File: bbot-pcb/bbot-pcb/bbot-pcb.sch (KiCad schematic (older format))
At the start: 11 parts, among them U1 HA-552-4P, U2 ADXL335, U3 HA-552-4P, U4 OPENLOG

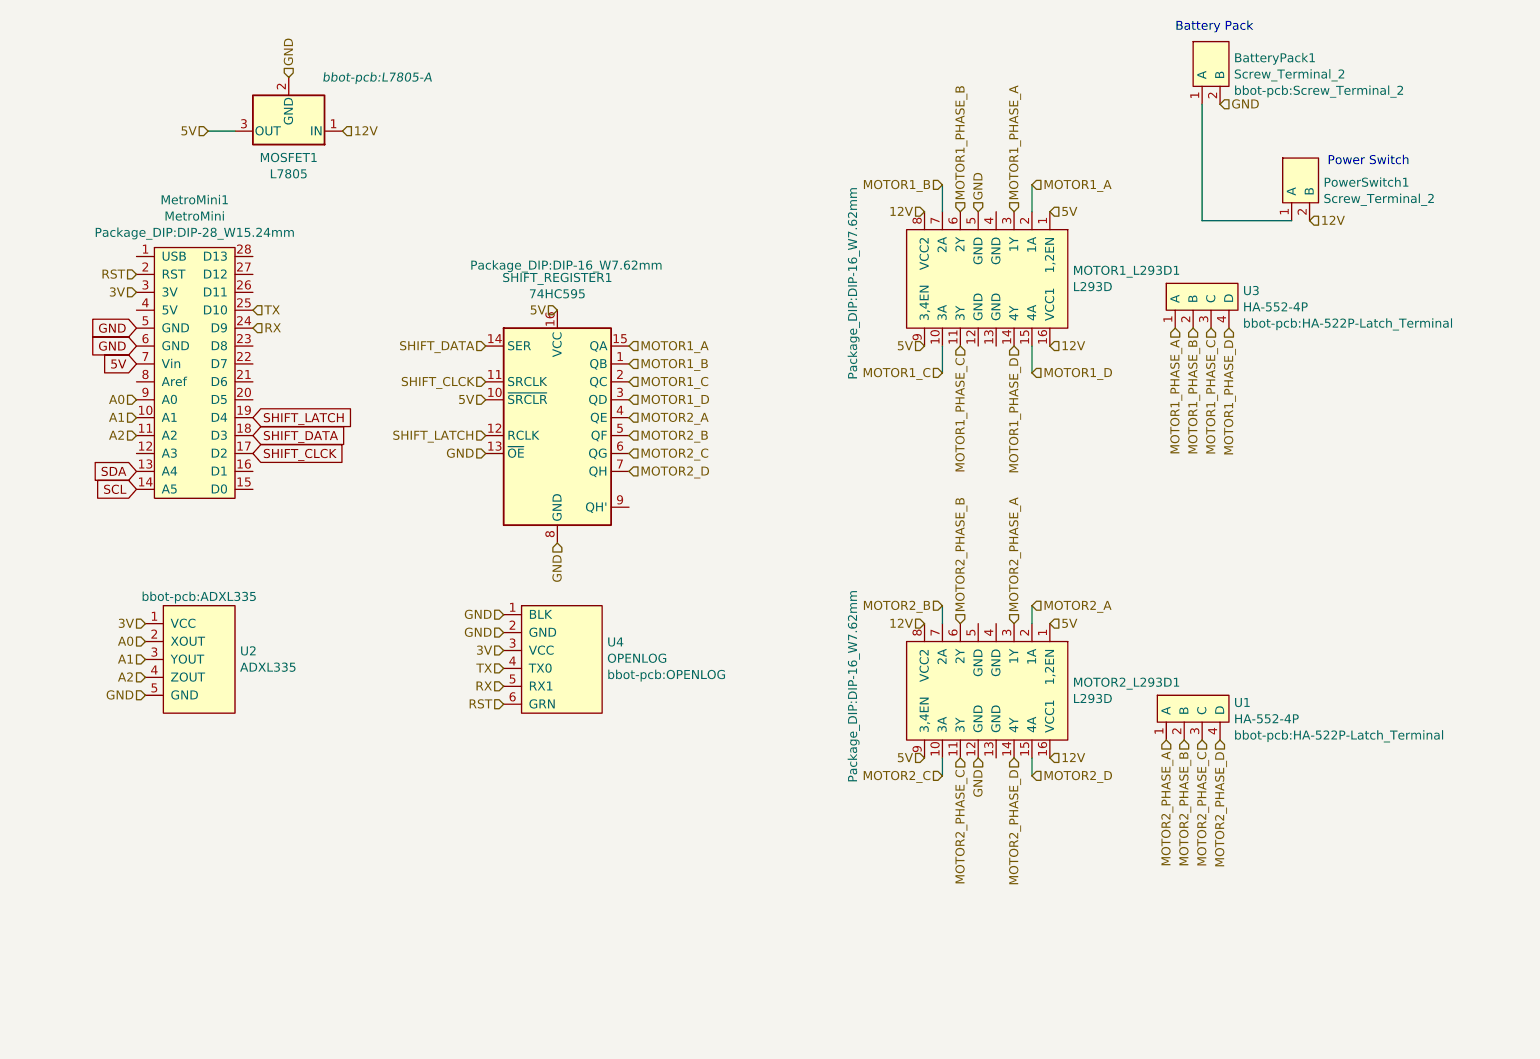
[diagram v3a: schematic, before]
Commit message: Update PCB to v3
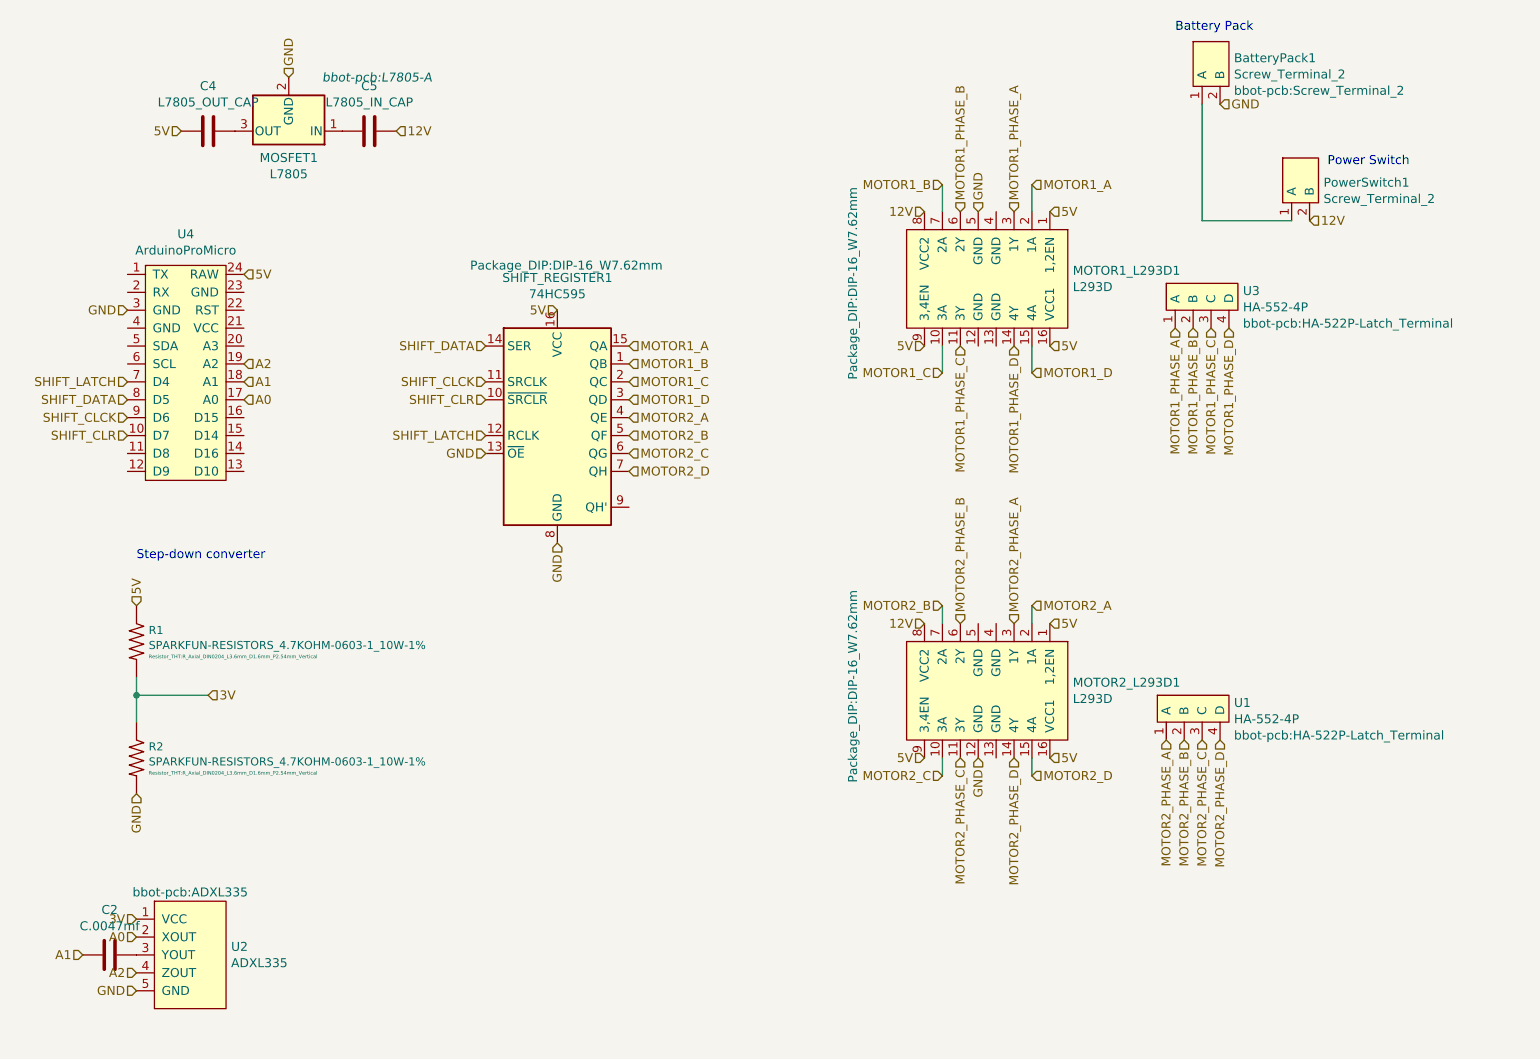
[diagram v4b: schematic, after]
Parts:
- removed MetroMini1: MetroMini, Package_DIP:DIP-28_W15.24mm, symbol bbot-component-library:MetroMini
- removed U4: OPENLOG, bbot-pcb:OPENLOG, symbol bbot-component-library:OPENLOG
- added C2: C.0047mf, Capacitor_THT:C_Disc_D3.4mm_W2.1mm_P2.50mm, symbol Device:C
- added C4: L7805_OUT_CAP, Capacitor_THT:CP_Radial_D5.0mm_P2.50mm, symbol Device:C
- added C5: L7805_IN_CAP, Capacitor_THT:CP_Radial_D5.0mm_P2.50mm, symbol Device:C
- added R1, R2: SPARKFUN-RESISTORS_4.7KOHM-0603-1_10W-1%, Resistor_THT:R_Axial_DIN0204_L3.6mm_D1.6mm_P2.54mm_Vertical, symbol Sparkfun:SPARKFUN-RESISTORS_4.7KOHM-0603-1_10W-1%
- added U4: ArduinoProMicro, promicro:ProMicro, symbol bbot-component-library:ArduinoProMicro
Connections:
- net 12V: now also C5.1; no longer MOSFET1.1 (IN), MOTOR1_L293D1.16 (VCC1), MOTOR2_L293D1.16 (VCC1)
- net 3V: now also R1.2, R2.1
- net 5V: now also MOTOR1_L293D1.16 (VCC1), MOTOR2_L293D1.16 (VCC1), C4.2, R1.1, U4.24 (RAW); no longer MOSFET1.3 (OUT), SHIFT_REGISTER1.10 (~SRCLR)
- net A0: now also U4.17 (A0)
- net A1: now also C2.2, U4.18 (A1); no longer U2.3 (YOUT)
- net A2: now also U4.19 (A2)
- net GND: now also R2.2, U4.3 (GND)
- net SHIFT_CLCK: now also U4.9 (D6)
- net SHIFT_DATA: now also U4.8 (D5)
- net SHIFT_LATCH: now also U4.7 (D4)
- new net: C5.2, MOSFET1.1 (IN)
- new net: C4.1, MOSFET1.3 (OUT)
- new net: C2.1, U2.3 (YOUT)
- new net SHIFT_CLR: SHIFT_REGISTER1.10 (~SRCLR), U4.10 (D7)
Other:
- note added: "Step-down converter"
- moved on the sheet: U2
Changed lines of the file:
@@
 Text HLabel 5900 1600 1    50   Input ~ 0
 GND
-Text HLabel 3550 3450 3    50   Input ~ 0
-GND
 Text HLabel 2050 850  1    50   Input ~ 0
 GND
-Text HLabel 2350 1150 2    50   Input ~ 0
+Text HLabel 2650 1150 2    50   Input ~ 0
 12V
 Text HLabel 6300 2350 2    50   Input ~ 0
-12V
+5V
 Text HLabel 5600 1600 0    50   Input ~ 0
 12V
 Text HLabel 6300 4650 2    50   Input ~ 0
-12V
+5V
 Text HLabel 5600 3900 0    50   Input ~ 0
 12V
-Wire Wire Line
-	1750 1150 1600 1150
-Text HLabel 1600 1150 0    50   Input ~ 0
+Text HLabel 1450 1150 0    50   Input ~ 0
 5V
 Text HLabel 3550 2150 0    50   Input ~ 0
@@
 SHIFT_CLCK
 Text HLabel 3150 2650 0    50   Input ~ 0
-5V
+SHIFT_CLR
 Text HLabel 3150 2950 0    50   Input ~ 0
 GND
@@
 Wire Wire Line
 	7150 1650 7650 1650
-$Comp
-L bbot-component-library:MetroMini MetroMini1
-U 1 1 6072CA85
-P 1550 2500
-F 0 "MetroMini1" H 1525 3465 50  0000 C CNN
-F 1 "MetroMini" H 1525 3374 50  0000 C CNN
-F 2 "Package_DIP:DIP-28_W15.24mm" H 1525 3283 50  0000 C CNN
-F 3 "" H 1300 2850 50  0001 C CNN
-	1    1550 2500
-	1    0    0    -1
-$EndComp
-Text GLabel 1200 2450 0    50   Input ~ 0
-5V
-Text GLabel 1850 2950 2    50   Input ~ 0
-SHIFT_CLCK
-Text GLabel 1850 2850 2    50   Input ~ 0
-SHIFT_DATA
-Text GLabel 1850 2750 2    50   Input ~ 0
-SHIFT_LATCH
-Text GLabel 1200 2250 0    50   Input ~ 0
-GND
-Text GLabel 1200 2350 0    50   Input ~ 0
-GND
-Text GLabel 1200 3050 0    50   Input ~ 0
-SDA
-Text GLabel 1200 3150 0    50   Input ~ 0
-SCL
 Wire Wire Line
 	5700 2350 5700 2500
@@
 L bbot-component-library:ADXL335 U2
 U 1 1 607BD863
-P 1500 3950
-F 0 "U2" H 1778 3846 50  0000 L CNN
-F 1 "ADXL335" H 1778 3755 50  0000 L CNN
-F 2 "bbot-pcb:ADXL335" H 1550 4150 50  0000 C CNN
-F 3 "" H 1250 4000 50  0001 C CNN
-	1    1500 3950
-	1    0    0    -1
-$EndComp
-Text HLabel 1250 3900 0    50   Input ~ 0
+P 1450 5600
+F 0 "U2" H 1728 5496 50  0000 L CNN
+F 1 "ADXL335" H 1728 5405 50  0000 L CNN
+F 2 "bbot-pcb:ADXL335" H 1500 5800 50  0000 C CNN
+F 3 "" H 1200 5650 50  0001 C CNN
+	1    1450 5600
+	1    0    0    -1
+$EndComp
+Text HLabel 1200 5550 0    50   Input ~ 0
 3V
-Text HLabel 1250 4000 0    50   Input ~ 0
+Text HLabel 1200 5650 0    50   Input ~ 0
 A0
-Text HLabel 1250 4100 0    50   Input ~ 0
+Text HLabel 900  5750 0    50   Input ~ 0
 A1
-Text HLabel 1250 4200 0    50   Input ~ 0
+Text HLabel 1200 5850 0    50   Input ~ 0
 A2
-Text HLabel 1250 4300 0    50   Input ~ 0
-GND
-Text HLabel 1200 2650 0    50   Input ~ 0
+Text HLabel 1200 5950 0    50   Input ~ 0
+GND
+Text HLabel 3550 3450 3    50   Input ~ 0
+GND
+$Comp
+L bbot-component-library:ArduinoProMicro U4
+U 1 1 608BA4F8
+P 1550 2450
+F 0 "U4" H 1475 3175 50  0000 C CNN
+F 1 "ArduinoProMicro" H 1475 3084 50  0000 C CNN
+F 2 "promicro:ProMicro" H 1250 3250 50  0001 C CNN
+F 3 "" H 1250 3250 50  0001 C CNN
+	1    1550 2450
+	1    0    0    -1
+$EndComp
+$Comp
+L Sparkfun:SPARKFUN-RESISTORS_4.7KOHM-0603-1_10W-1% R1
+U 1 1 608BCB4A
+P 1200 4000
+F 0 "R1" V 1137 4068 45  0000 L CNN
+F 1 "SPARKFUN-RESISTORS_4.7KOHM-0603-1_10W-1%" V 1221 4068 45  0000 L CNN
+F 2 "Resistor_THT:R_Axial_DIN0204_L3.6mm_D1.6mm_P2.54mm_Vertical" V 1284 4068 20  0000 L CNN
+F 3 "" H 1200 4000 60  0001 C CNN
+	1    1200 4000
+	0    1    1    0
+$EndComp
+$Comp
+L Sparkfun:SPARKFUN-RESISTORS_4.7KOHM-0603-1_10W-1% R2
+U 1 1 608BDF88
+P 1200 4650
+F 0 "R2" V 1137 4718 45  0000 L CNN
+F 1 "SPARKFUN-RESISTORS_4.7KOHM-0603-1_10W-1%" V 1221 4718 45  0000 L CNN
+F 2 "Resistor_THT:R_Axial_DIN0204_L3.6mm_D1.6mm_P2.54mm_Vertical" V 1284 4718 20  0000 L CNN
+F 3 "" H 1200 4650 60  0001 C CNN
+	1    1200 4650
+	0    1    1    0
+$EndComp
+Text HLabel 1200 4850 3    50   Input ~ 0
+GND
+Text HLabel 1200 3800 1    50   Input ~ 0
+5V
+Wire Wire Line
+	1200 4200 1200 4300
+Wire Wire Line
+	1200 4300 1600 4300
+Connection ~ 1200 4300
+Wire Wire Line
+	1200 4300 1200 4450
+Text HLabel 1600 4300 2    50   Input ~ 0
+3V
+Text HLabel 1800 1950 2    50   Input ~ 0
+5V
+Text HLabel 1150 2150 0    50   Input ~ 0
+GND
+Text HLabel 1800 2650 2    50   Input ~ 0
 A0
-Text HLabel 1200 2750 0    50   Input ~ 0
+Text HLabel 1800 2550 2    50   Input ~ 0
 A1
-Text HLabel 1200 2850 0    50   Input ~ 0
+Text HLabel 1800 2450 2    50   Input ~ 0
 A2
-Text HLabel 1200 2050 0    50   Input ~ 0
-3V
-$Comp
-L bbot-component-library:OPENLOG U4
-U 1 1 607C091B
-P 3550 4050
-F 0 "U4" H 3828 4096 50  0000 L CNN
-F 1 "OPENLOG" H 3828 4005 50  0000 L CNN
-F 2 "bbot-pcb:OPENLOG" H 3828 3914 50  0000 L CNN
-F 3 "" H 3250 4250 50  0001 C CNN
-	1    3550 4050
-	1    0    0    -1
-$EndComp
-Text HLabel 3250 4050 0    50   Input ~ 0
-3V
-Text HLabel 3250 3950 0    50   Input ~ 0
-GND
-Text HLabel 3250 3850 0    50   Input ~ 0
-GND
-Text HLabel 3250 4150 0    50   Input ~ 0
-TX
-Text HLabel 3250 4250 0    50   Input ~ 0
-RX
-Text HLabel 1850 2150 2    50   Input ~ 0
-TX
-Text HLabel 1850 2250 2    50   Input ~ 0
-RX
-Text HLabel 3250 4350 0    50   Input ~ 0
-RST
-Text HLabel 1200 1950 0    50   Input ~ 0
-RST
+Text Notes 1200 3550 0    50   ~ 0
+Step-down converter
+Text HLabel 1150 2550 0    50   Input ~ 0
+SHIFT_LATCH
+Text HLabel 1150 2650 0    50   Input ~ 0
+SHIFT_DATA
+Text HLabel 1150 2750 0    50   Input ~ 0
+SHIFT_CLCK
+Text HLabel 1150 2850 0    50   Input ~ 0
+SHIFT_CLR
+$Comp
+L Device:C C2
+U 1 1 608C7BCB
+P 1050 5750
+F 0 "C2" V 798 5750 50  0000 C CNN
+F 1 "C.0047mf" V 889 5750 50  0000 C CNN
+F 2 "Capacitor_THT:C_Disc_D3.4mm_W2.1mm_P2.50mm" H 1088 5600 50  0001 C CNN
+F 3 "~" H 1050 5750 50  0001 C CNN
+	1    1050 5750
+	0    1    1    0
+$EndComp
+$Comp
+L Device:C C4
+U 1 1 608C879A
+P 1600 1150
+F 0 "C4" V 1348 1150 50  0000 C CNN
+F 1 "L7805_OUT_CAP" V 1439 1150 50  0000 C CNN
+F 2 "Capacitor_THT:CP_Radial_D5.0mm_P2.50mm" H 1638 1000 50  0001 C CNN
+F 3 "~" H 1600 1150 50  0001 C CNN
+	1    1600 1150
+	0    1    1    0
+$EndComp
+$Comp
+L Device:C C5
+U 1 1 608C9E4F
+P 2500 1150
+F 0 "C5" V 2248 1150 50  0000 C CNN
+F 1 "L7805_IN_CAP" V 2339 1150 50  0000 C CNN
+F 2 "Capacitor_THT:CP_Radial_D5.0mm_P2.50mm" H 2538 1000 50  0001 C CNN
+F 3 "~" H 2500 1150 50  0001 C CNN
+	1    2500 1150
+	0    1    1    0
+$EndComp
 $EndSCHEMATC

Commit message: RElease-candidate of models and pcb
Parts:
- C4, C5: footprint Capacitor_THT:CP_Radial_D5.0mm_P2.50mm -> Capacitor_THT:C_Disc_D4.3mm_W1.9mm_P5.00mm
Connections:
- net 12V: now also MOSFET1.1 (IN)
- net 5V: now also C4.1, MOSFET1.3 (OUT); no longer C4.2
- net A1: now also C2.1, U2.3 (YOUT); no longer C2.2
- net GND: now also C2.2, C4.2, C5.2
- net SHIFT_CLCK: now also U4.8 (D5); no longer U4.9 (D6)
- net SHIFT_CLR: now also U4.7 (D4); no longer U4.10 (D7)
- net SHIFT_DATA: now also U4.10 (D7); no longer U4.8 (D5)
- net SHIFT_LATCH: now also U4.9 (D6); no longer U4.7 (D4)
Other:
- moved on the sheet: C2, C4, C5
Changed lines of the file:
@@
 Text HLabel 5600 3900 0    50   Input ~ 0
 12V
-Text HLabel 1450 1150 0    50   Input ~ 0
+Text HLabel 1550 1150 0    50   Input ~ 0
 5V
 Text HLabel 3550 2150 0    50   Input ~ 0
@@
 Text HLabel 1200 5650 0    50   Input ~ 0
 A0
-Text HLabel 900  5750 0    50   Input ~ 0
+Text HLabel 700  5700 0    50   Input ~ 0
 A1
 Text HLabel 1200 5850 0    50   Input ~ 0
@@
 Text Notes 1200 3550 0    50   ~ 0
 Step-down converter
+Text HLabel 1150 2750 0    50   Input ~ 0
+SHIFT_LATCH
+Text HLabel 1150 2850 0    50   Input ~ 0
+SHIFT_DATA
+Text HLabel 1150 2650 0    50   Input ~ 0
+SHIFT_CLCK
 Text HLabel 1150 2550 0    50   Input ~ 0
-SHIFT_LATCH
-Text HLabel 1150 2650 0    50   Input ~ 0
-SHIFT_DATA
-Text HLabel 1150 2750 0    50   Input ~ 0
-SHIFT_CLCK
-Text HLabel 1150 2850 0    50   Input ~ 0
 SHIFT_CLR
 $Comp
 L Device:C C2
 U 1 1 608C7BCB
-P 1050 5750
-F 0 "C2" V 798 5750 50  0000 C CNN
-F 1 "C.0047mf" V 889 5750 50  0000 C CNN
-F 2 "Capacitor_THT:C_Disc_D3.4mm_W2.1mm_P2.50mm" H 1088 5600 50  0001 C CNN
-F 3 "~" H 1050 5750 50  0001 C CNN
-	1    1050 5750
-	0    1    1    0
+P 900 5850
+F 0 "C2" V 648 5850 50  0000 C CNN
+F 1 "C.0047mf" V 739 5850 50  0000 C CNN
+F 2 "Capacitor_THT:C_Disc_D3.4mm_W2.1mm_P2.50mm" H 938 5700 50  0001 C CNN
+F 3 "~" H 900 5850 50  0001 C CNN
+	1    900  5850
+	1    0    0    -1
 $EndComp
 $Comp
 L Device:C C4
 U 1 1 608C879A
-P 1600 1150
-F 0 "C4" V 1348 1150 50  0000 C CNN
-F 1 "L7805_OUT_CAP" V 1439 1150 50  0000 C CNN
-F 2 "Capacitor_THT:CP_Radial_D5.0mm_P2.50mm" H 1638 1000 50  0001 C CNN
-F 3 "~" H 1600 1150 50  0001 C CNN
-	1    1600 1150
-	0    1    1    0
+P 1600 1300
+F 0 "C4" V 1348 1300 50  0000 C CNN
+F 1 "L7805_OUT_CAP" V 1250 1300 50  0000 C CNN
+F 2 "Capacitor_THT:C_Disc_D4.3mm_W1.9mm_P5.00mm" H 1638 1150 50  0001 C CNN
+F 3 "~" H 1600 1300 50  0001 C CNN
+	1    1600 1300
+	1    0    0    -1
 $EndComp
 $Comp
 L Device:C C5
 U 1 1 608C9E4F
-P 2500 1150
-F 0 "C5" V 2248 1150 50  0000 C CNN
-F 1 "L7805_IN_CAP" V 2339 1150 50  0000 C CNN
-F 2 "Capacitor_THT:CP_Radial_D5.0mm_P2.50mm" H 2538 1000 50  0001 C CNN
-F 3 "~" H 2500 1150 50  0001 C CNN
-	1    2500 1150
-	0    1    1    0
-$EndComp
+P 2550 1300
+F 0 "C5" V 2298 1300 50  0000 C CNN
+F 1 "L7805_IN_CAP" V 2400 1100 50  0000 C CNN
+F 2 "Capacitor_THT:C_Disc_D4.3mm_W1.9mm_P5.00mm" H 2588 1150 50  0001 C CNN
+F 3 "~" H 2550 1300 50  0001 C CNN
+	1    2550 1300
+	1    0    0    -1
+$EndComp
+Text HLabel 1600 1450 0    50   Input ~ 0
+GND
+Text HLabel 2550 1450 2    50   Input ~ 0
+GND
+Wire Wire Line
+	1550 1150 1600 1150
+Wire Wire Line
+	1600 1150 1750 1150
+Connection ~ 1600 1150
+Wire Wire Line
+	2350 1150 2550 1150
+Wire Wire Line
+	2550 1150 2650 1150
+Connection ~ 2550 1150
+Wire Wire Line
+	700  5700 900  5700
+Wire Wire Line
+	900  5700 1000 5700
+Wire Wire Line
+	1000 5700 1000 5750
+Wire Wire Line
+	1000 5750 1200 5750
+Connection ~ 900  5700
+Text HLabel 900  6000 3    50   Input ~ 0
+GND
 $EndSCHEMATC
